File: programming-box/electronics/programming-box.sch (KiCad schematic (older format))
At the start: 14 parts, among them K1 CONN_3, P1 CONN_2, P2 CONN_2, P3 CONN_2, SW1 BACK, SW2 OK, SW3 UP, SW4 DOWN, SW5 LEFT, SW6 RIGHT, U1 LIPO_CHARGER_+_PROTECTION, U2 STM32F103C8T6_DEV_BOARD, U3 TFT-1.8-128X160-SPI, U4 NRF24L01P

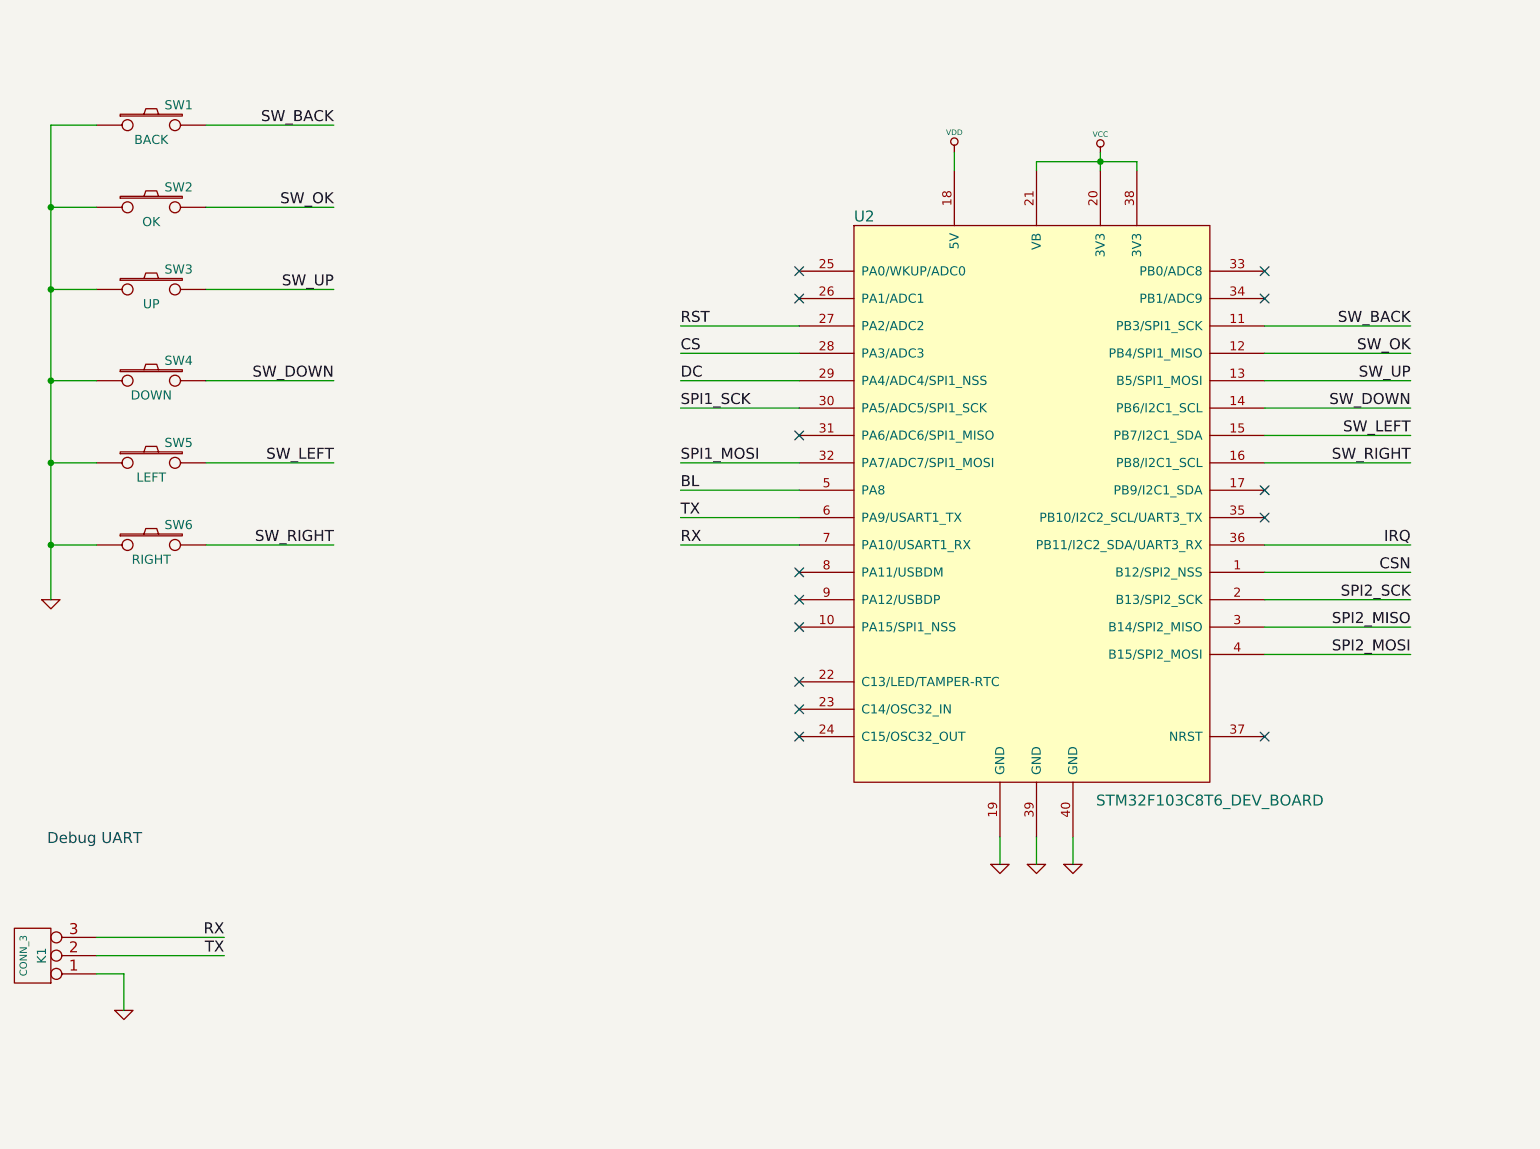
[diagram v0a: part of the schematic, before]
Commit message: Add PCB (breadboard simulation) draft.
Adjust pin-out according to best fit
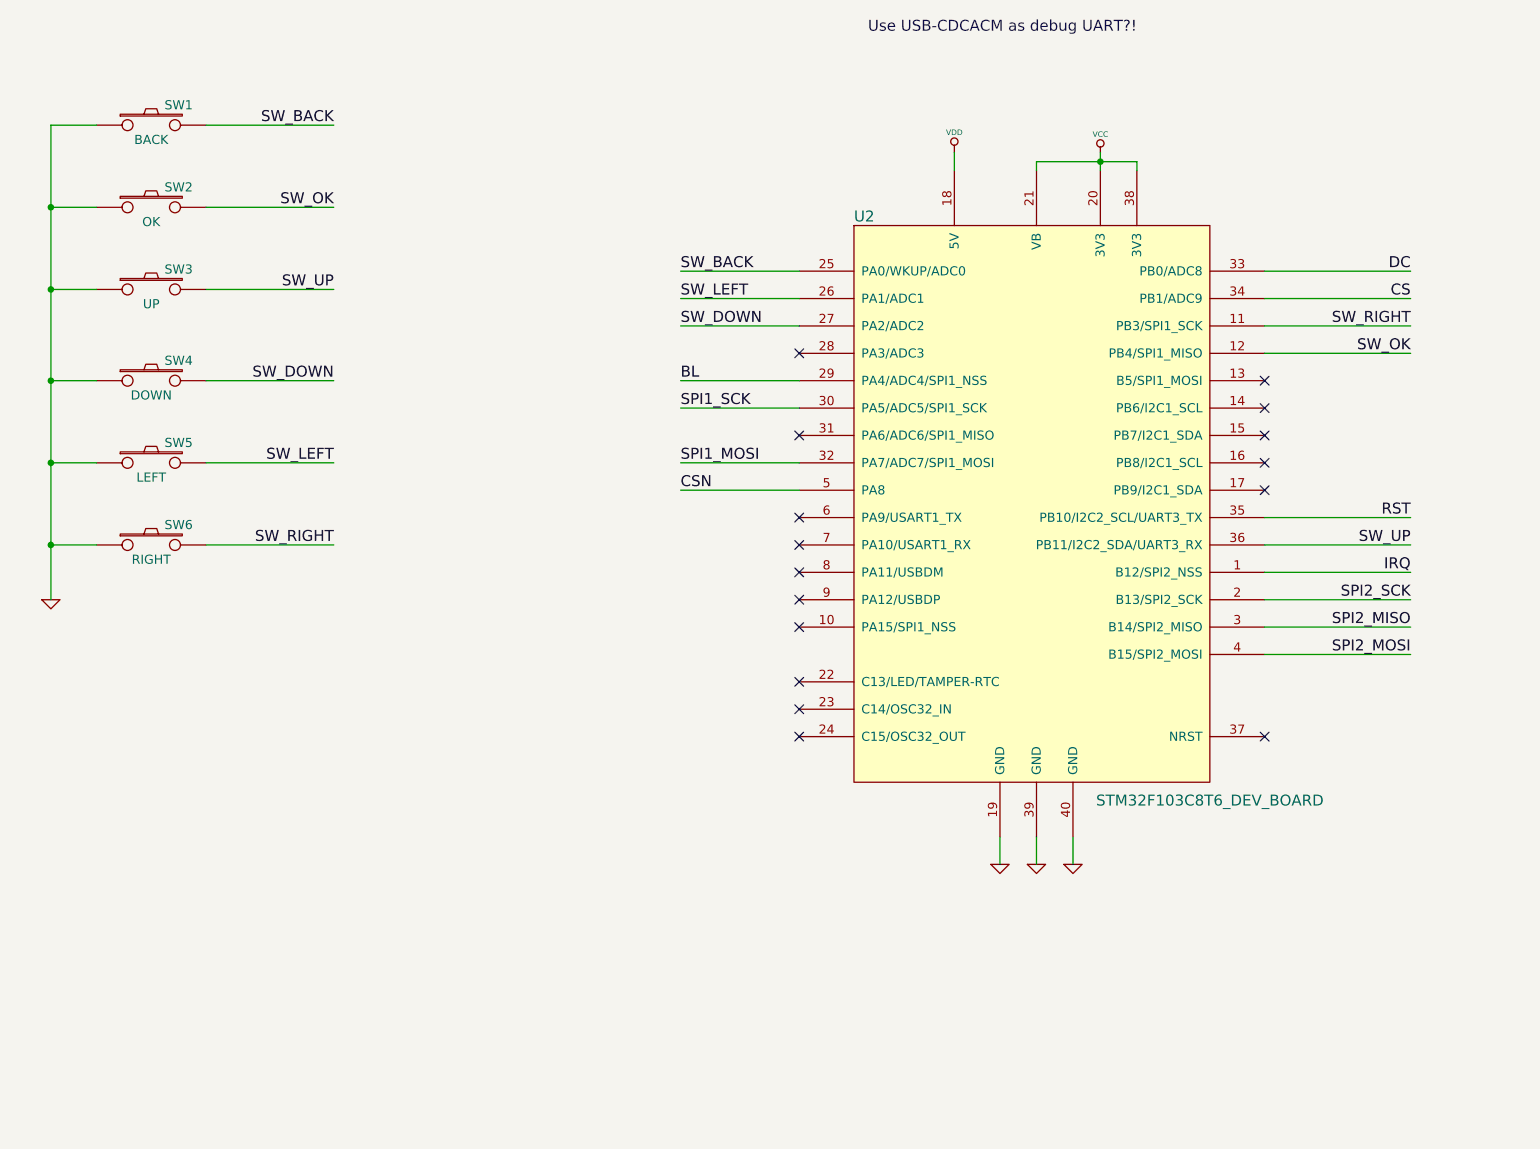
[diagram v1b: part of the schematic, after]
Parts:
- removed K1: CONN_3, symbol CONN_3
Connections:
- net BL: now also U2.29 (PA4/ADC4/SPI1_NSS); no longer U2.5 (PA8)
- net CS: now also U2.34 (PB1/ADC9); no longer U2.28 (PA3/ADC3)
- net CSN: now also U2.5 (PA8); no longer U2.1 (B12/SPI2_NSS)
- net DC: now also U2.33 (PB0/ADC8); no longer U2.29 (PA4/ADC4/SPI1_NSS)
- net IRQ: now also U2.1 (B12/SPI2_NSS); no longer U2.36 (PB11/I2C2_SDA/UART3_RX)
- net RST: now also U2.35 (PB10/I2C2_SCL/UART3_TX); no longer U2.27 (PA2/ADC2)
- net SW_BACK: now also U2.25 (PA0/WKUP/ADC0); no longer U2.11 (PB3/SPI1_SCK)
- net SW_DOWN: now also U2.27 (PA2/ADC2); no longer U2.14 (PB6/I2C1_SCL)
- net SW_LEFT: now also U2.26 (PA1/ADC1); no longer U2.15 (PB7/I2C1_SDA)
- net SW_RIGHT: now also U2.11 (PB3/SPI1_SCK); no longer U2.16 (PB8/I2C1_SCL)
- net SW_UP: now also U2.36 (PB11/I2C2_SDA/UART3_RX); no longer U2.13 (B5/SPI1_MOSI)
- net RX: no longer names the net of U2.7 (PA10/USART1_RX)
- net TX: no longer names the net of U2.6 (PA9/USART1_TX)
- no-connect marks 16 -> 18
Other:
- note added: "Use USB-CDCACM as debug UART?!"
- note removed: "Debug UART"
